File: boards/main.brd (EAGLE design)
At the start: 25.4 x 25.4 mm, 24 parts, among them T1 PMBT4401,215, T2 PMBT4401,215, U1 MCP1703T-3002E/CB, X1 DF13-4P-1.25V(50), X2 DF13-4P-1.25V(50)

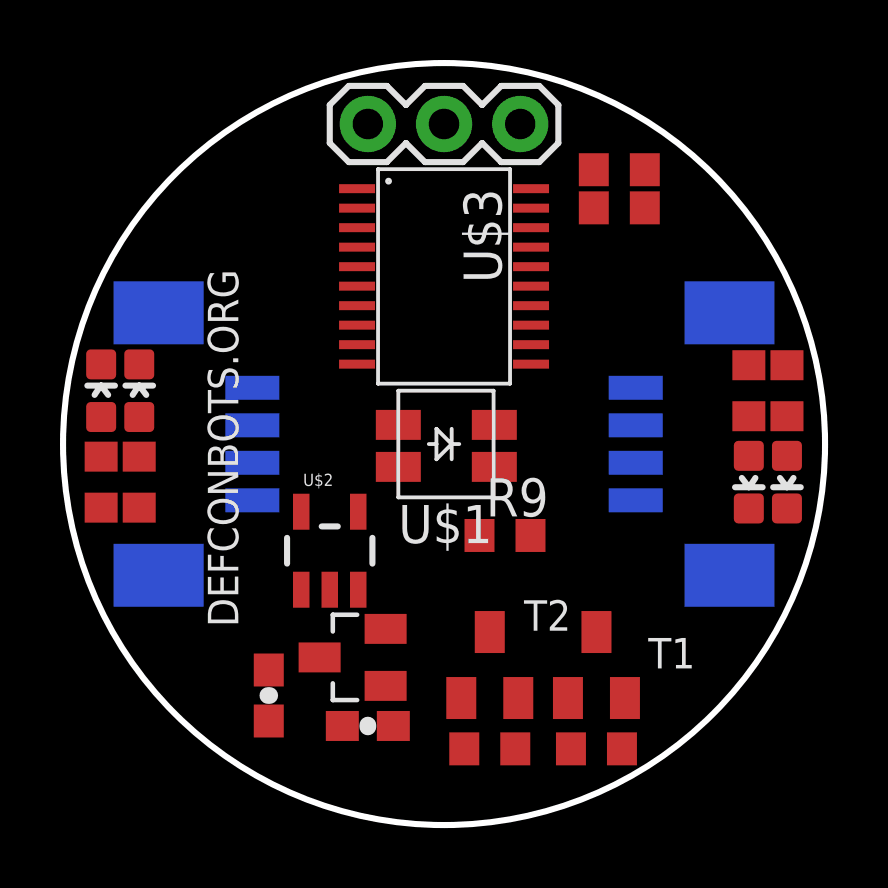
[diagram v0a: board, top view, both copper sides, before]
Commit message: Rough schematic, aproximate placement.
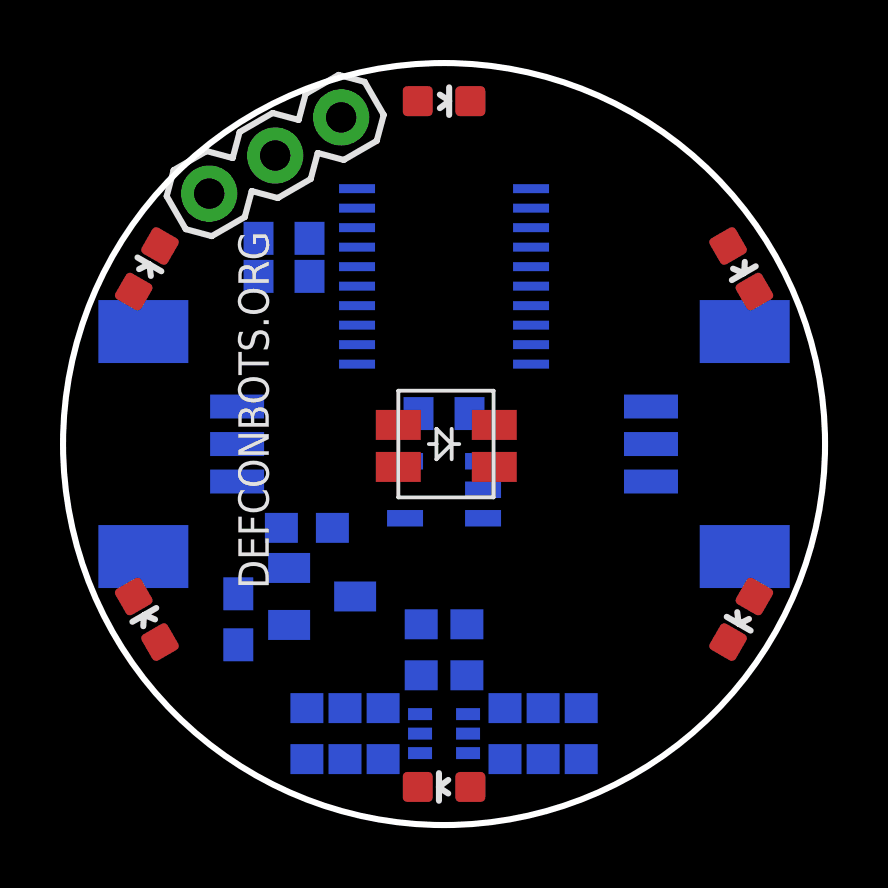
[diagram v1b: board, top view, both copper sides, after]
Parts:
- removed T1, T2: PMBT4401,215, transistor:SOT23-BEC
- removed X1, X2: DF13-4P-1.25V(50), con-molex:53398-04
- added D5: VLMB1300-GS08, SparkFun-LED:LED-0603
- added D6: VLMS1300-GS08, SparkFun-LED:LED-0603
- added Q1: BC847BS, transistor-small-signal:SOT363_PHILIPS
- added R10, R11: CRCW0603200RFKEA, rcl:R0603
- added X3, X4: 53398-03, con-molex:53398-03
- moved R4 16.9 mm to (16.0, 3.05), flipped to the bottom, turned to 90 degrees
- moved R6 16.7 mm to (10.7, 3.05), flipped to the bottom, turned to 270 degrees
- moved D4 14.0 mm to (12.7, 24.1), turned to 270 degrees
- moved R3 13.3 mm to (17.3, 3.05), flipped to the bottom
- moved R1 11.4 mm to (7.37, 18.3), flipped to the bottom
- moved R2 11.4 mm to (7.37, 19.6), flipped to the bottom
- moved R7 10.1 mm to (8.13, 3.05), flipped to the bottom
- moved D1 7.27 mm to (22.6, 18.5), turned to 210 degrees
- moved C2 6.91 mm to (8.13, 9.91), flipped to the bottom
- moved R5 6.71 mm to (11.9, 5.84), flipped to the bottom, turned to 90 degrees
- moved JP1 5.97 mm to (9.27, 23.6), turned to 210 degrees
- moved D3 4.58 mm to (22.6, 6.86), turned to 150 degrees
- moved R9 4.54 mm to (12.7, 13.7), flipped to the bottom
- moved D2 4.34 mm to (2.79, 18.5), turned to 330 degrees
- moved U$2 4.32 mm to (12.7, 11.2), flipped to the bottom, turned to 270 degrees
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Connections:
- removed net N$18: R5.1, T1.B
- removed net N$3: R9.1, U$2.1
- new net N$11: Q1.5, R8.1
- new net N$8: D3.C, R6.2
- new net N$9: D4.C, R7.2
- net +3V3: now also D1.A, D2.A, D3.A, D4.A, D5.A, D6.A; no longer R3.2, R4.2, R6.2, R7.2
- net GND: now also Q1.1, Q1.4, X3.3, X4.3; no longer T1.E, T2.E, X1.2, X2.2
- net LED: now also Q1.6, R10.1, R3.1, R4.1; no longer D1.C, D2.C, T1.C
- net N$1: now also D1.C, R3.2; no longer D4.A, R7.1
- net N$10: now also D6.C, R11.2; no longer D3.A, R6.1
- net N$2: now also Q1.3, R11.1, R6.1, R7.1; no longer D3.C, D4.C, T2.C
- net N$4: now also Q1.2, R5.1; no longer R8.1, T2.B
- net N$6: now also D2.C, R4.2; no longer D2.A, R4.1
- net N$7: now also D5.C, R10.2; no longer D1.A, R3.1
- net RX: now also R9.1, U$2.1; no longer X1.3, X2.3
- net TX: now also X3.2, X4.2; no longer X1.4, X2.4
- net VIN: now also X3.1, X4.1; no longer X1.1, X2.1

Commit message: Swap msp430 for LPC8* arm processor. Add battery/controller-radio board
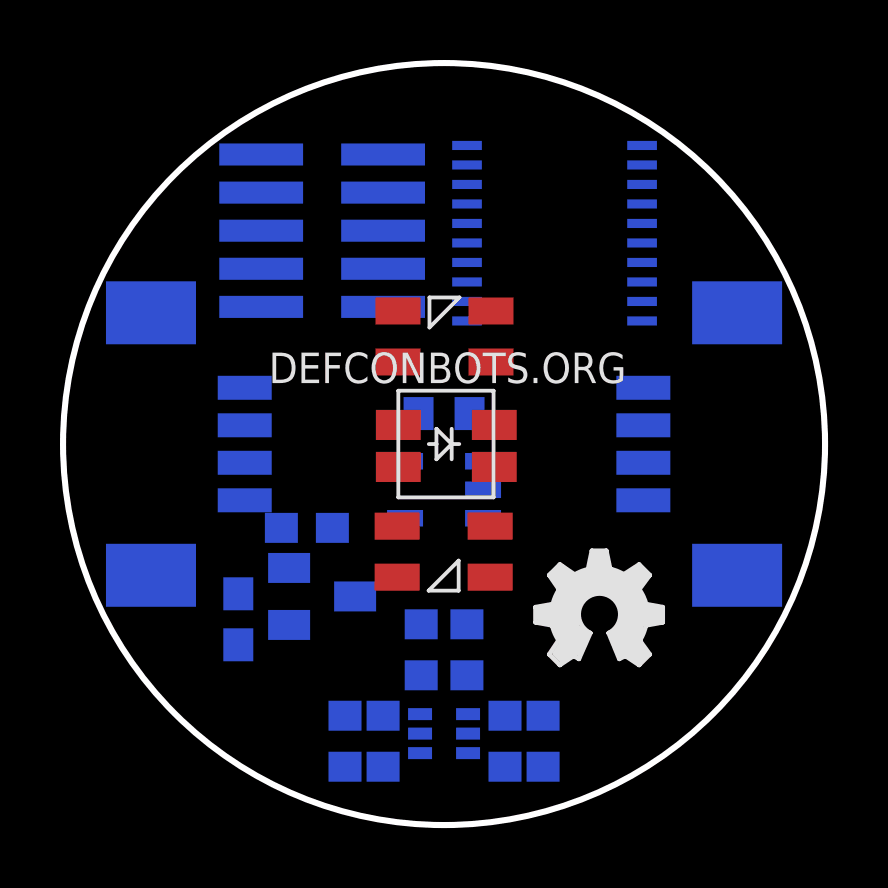
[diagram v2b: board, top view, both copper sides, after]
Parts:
- removed D1, D2, D5: VLMB1300-GS08, SparkFun-LED:LED-0603
- removed D3, D4, D6: VLMS1300-GS08, SparkFun-LED:LED-0603
- removed JP1: (no value), SparkFun-Connectors:1X03
- removed R10, R4, R6, R7: CRCW0603200RFKEA, rcl:R0603
- removed X3, X4: 53398-03, con-molex:53398-03
- added LOGO2: OSHW_LOGO_FILLX0150-NT, ohw-logo:OSHW_FILLX150_NOTEXT
- added LPC812: LPC812M101JDH20, LPC800:TSSOP20
- added U$4, U$5: 150141RB73100, torpedo:150141RB
- added X1, X2: 53398-04, con-molex:53398-04
- R1, R2: value RK73H1JTTD4702F -> CRCW0603200RFKEA
- U$3: value MSP430G2433 -> FTSH-105; device torpedo:PW20 -> torpedo:FTSH-105-01-XXX-DV-K
- moved R1 17.7 mm to (16.0, 2.79), turned to 90 degrees
- moved R2 16.9 mm to (9.40, 2.79), turned to 270 degrees
- moved U$3 4.34 mm to (8.64, 19.8), turned to 90 degrees
- moved R3 2.55 mm to (14.7, 2.79)
- moved R11 1.30 mm to (10.7, 2.79)
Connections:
- removed net LED: Q1.6, R10.1, R3.1, R4.1
- removed net N$10: D6.C, R11.2
- removed net N$9: D4.C, R7.2
- removed net TEST: JP1.1, R2.2, U$3.17
- new net LASER_RX: LPC812.3, R9.1, U$2.1
- new net N$3: R11.2, U$4.3
- new net SWCLK: LPC812.6, U$3.4
- new net SWDIO: LPC812.7, U$3.2
- net +3V3: now also LPC812.15, U$4.1, U$4.2, U$5.1, U$5.2; no longer D1.A, D2.A, D3.A, D4.A, D5.A, D6.A, R1.2
- net BLUE_LED: now also LPC812.1; no longer U$3.5
- net GND: now also LPC812.16, U$3.3, U$3.5, U$3.9, X1.4, X2.4; no longer JP1.3, R2.1, U$3.20, X3.3, X4.3
- net N$1: now also Q1.6, R1.1, R3.1; no longer D1.C, R3.2
- net N$2: now also R2.1; no longer R6.1, R7.1
- net N$6: now also R2.2, U$5.3; no longer D2.C, R4.2
- net N$7: now also R1.2, U$4.4; no longer D5.C, R10.2
- net N$8: now also R3.2, U$5.4; no longer D3.C, R6.2
- net RED_LED: now also LPC812.10; no longer U$3.6
- net RST: now also LPC812.4, U$3.10; no longer JP1.2, R1.1, U$3.16
- net RX: now also LPC812.8, X1.3, X2.3; no longer R9.1, U$2.1, U$3.3
- net TX: now also LPC812.9, X1.2, X2.2; no longer U$3.4, X3.2, X4.2
- net VIN: now also X1.1, X2.1; no longer X3.1, X4.1
